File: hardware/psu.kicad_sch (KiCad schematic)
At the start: 35 parts, among them J6 12V Screw Terminal, J7 12V Barrel, Q1 FDS4435BZ, U5 NCP1117-3.3_SOT223, U6 AP64501SP-13

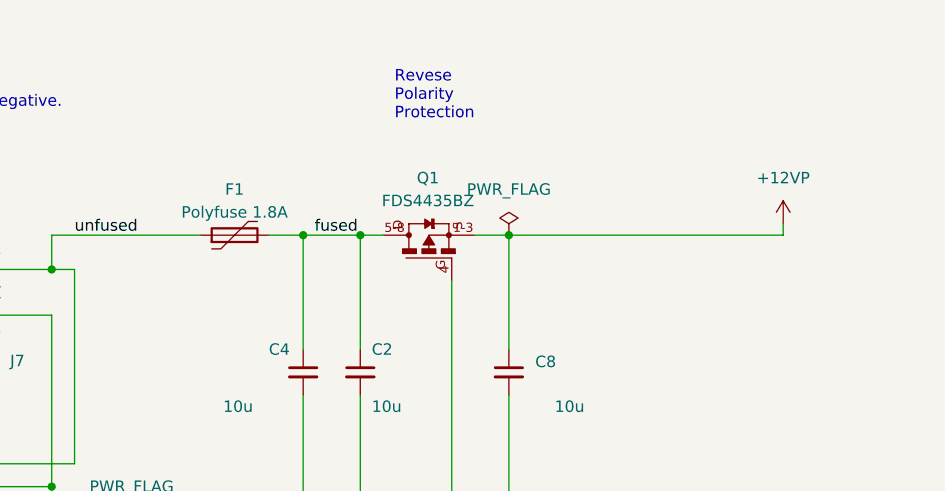
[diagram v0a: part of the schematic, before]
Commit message: PSU: replace polyfuse with SMD fuse (Device:Fuse)
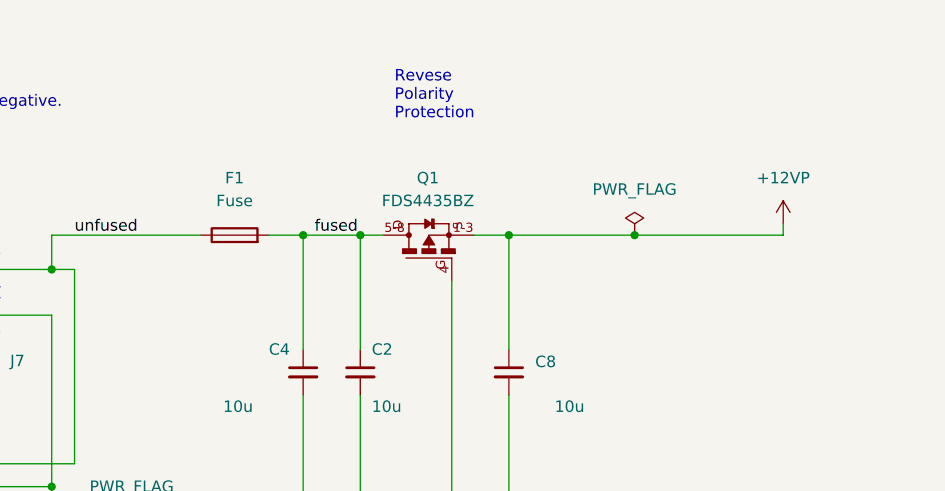
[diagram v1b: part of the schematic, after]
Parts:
- removed F1: Polyfuse 1.8A, Fuse:Fuse_1812_4532Metric, symbol Device:Polyfuse
- added F1: Fuse, symbol Device:Fuse
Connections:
- net fused: now also F1.2
- net unfused: now also F1.1
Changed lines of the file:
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@@
 	)
 	(junction
+		(at 116.84 44.45)
+		(diameter 0)
+		(color 0 0 0 0)
+	)
+	(junction
 		(at 212.09 48.26)
 		(diameter 0)
@@
 	(wire
 		(pts
+			(xy 116.84 44.45) (xy 133.35 44.45)
+		)
+		(stroke
+			(width 0)
+			(type default)
+		)
+	)
+	(wire
+		(pts
 			(xy 179.07 113.03) (xy 179.07 119.38)
 		)
@@
 	(wire
 		(pts
-			(xy 102.87 44.45) (xy 133.35 44.45)
+			(xy 102.87 44.45) (xy 116.84 44.45)
 		)
 		(stroke
@@
 	(symbol
 		(lib_id "power:PWR_FLAG")
-		(at 102.87 44.45 0)
+		(at 116.84 44.45 0)
 		(unit 1)
 		(body_style 1)
@@
 		(fields_autoplaced yes)
 		(property "Reference" "#FLG02"
-			(at 102.87 42.545 0)
+			(at 116.84 42.545 0)
 			(hide yes)
 			(show_name no)
@@
 		)
 		(property "Value" "PWR_FLAG"
-			(at 102.87 39.37 0)
+			(at 116.84 39.37 0)
 			(show_name no)
 			(do_not_autoplace no)
@@
 		)
 		(property "Footprint" ""
-			(at 102.87 44.45 0)
+			(at 116.84 44.45 0)
 			(hide yes)
 			(show_name no)
@@
 		)
 		(property "Datasheet" ""
-			(at 102.87 44.45 0)
+			(at 116.84 44.45 0)
 			(hide yes)
 			(show_name no)
@@
 		)
 		(property "Description" "Special symbol for telling ERC where power comes from"
-			(at 102.87 44.45 0)
+			(at 116.84 44.45 0)
 			(hide yes)
 			(show_name no)
@@
 	)
 	(symbol
-		(lib_id "Device:R_Small")
-		(at 168.91 137.16 0)
+		(lib_id "Device:Fuse")
+		(at 72.39 44.45 90)
 		(unit 1)
 		(body_style 1)
@@
 		(in_pos_files yes)
 		(dnp no)
-		(property "Reference" "R14"
-			(at 170.688 135.9916 0)
+		(fields_autoplaced yes)
+		(property "Reference" "F1"
+			(at 72.39 38.1 90)
 			(show_name no)
 			(do_not_autoplace no)
@@
 					(size 1.27 1.27)
 				)
-				(justify left)
 			)
 		)
-		(property "Value" "20K"
-			(at 170.688 138.303 0)
+		(property "Value" "Fuse"
+			(at 72.39 40.64 90)
 			(show_name no)
 			(do_not_autoplace no)
@@
 					(size 1.27 1.27)
 				)
-				(justify left)
 			)
 		)
-		(property "Footprint" "Resistor_SMD:R_0805_2012Metric"
-			(at 167.132 137.16 90)
+		(property "Footprint" ""
+			(at 72.39 46.228 90)
 			(hide yes)
 			(show_name no)
@@
 		)
 		(property "Datasheet" ""
-			(at 168.91 137.16 0)
-			(hide yes)
-			(show_name no)
-			(do_not_autoplace no)
-			(effects
-				(font
-					(size 1.27 1.27)
-				)
-			)
-		)
-		(property "Description" "Resistor, small symbol"
-			(at 168.91 137.16 0)
-			(hide yes)
-			(show_name no)
-			(do_not_autoplace no)
-			(effects
-				(font
-					(size 1.27 1.27)
-				)
-			)
-		)
-		(property "Notes" "Resistor 20K 1% 63mW"
-			(at 168.91 137.16 0)
+			(at 72.39 44.45 0)
 			(hide yes)
 			(show_name no)
@@
 			)
 		)
-		(property "Supplier" "https://www.digikey.ch/de/products/detail/stackpole-electronics-inc/RMCF0805FT20K0/1760314"
-			(at 168.91 137.16 0)
+		(property "Description" "Fuse"
+			(at 72.39 44.45 0)
 			(hide yes)
 			(show_name no)
@@
 			(project "granit"
 				(path "/d2c135e3-a983-4cd4-8cff-b50ca3c7671a/5c34f141-50d5-4609-a101-f9d94643eff8"
-					(reference "R14")
+					(reference "F1")
 					(unit 1)
 				)
@@
 	)
 	(symbol
-		(lib_id "Device:C_Small")
-		(at 86.36 130.81 0)
+		(lib_id "Device:R_Small")
+		(at 168.91 137.16 0)
 		(unit 1)
 		(body_style 1)
@@
 		(in_pos_files yes)
 		(dnp no)
-		(property "Reference" "C6"
-			(at 89.281 129.6416 0)
+		(property "Reference" "R14"
+			(at 170.688 135.9916 0)
 			(show_name no)
 			(do_not_autoplace no)
@@
 			)
 		)
-		(property "Value" "10u"
-			(at 82.55 136.398 0)
+		(property "Value" "20K"
+			(at 170.688 138.303 0)
 			(show_name no)
 			(do_not_autoplace no)
@@
 			)
 		)
-		(property "Footprint" "Capacitor_SMD:C_0805_2012Metric"
-			(at 87.3252 134.62 0)
+		(property "Footprint" "Resistor_SMD:R_0805_2012Metric"
+			(at 167.132 137.16 90)
 			(hide yes)
 			(show_name no)
@@
 			)
 		)
-		(property "Datasheet" "https://www.samsungsem.com/resources/file/global/support/product_catalog/MLCC.pdf"
-			(at 86.36 130.81 0)
+		(property "Datasheet" ""
+			(at 168.91 137.16 0)
 			(hide yes)
 			(show_name no)
@@
 			)
 		)
-		(property "Description" ""
-			(at 86.36 130.81 0)
+		(property "Description" "Resistor, small symbol"
+			(at 168.91 137.16 0)
 			(hide yes)
 			(show_name no)
@@
 			)
 		)
-		(property "Supplier" "https://www.digikey.ch/de/products/detail/samsung-electro-mechanics/CL21X106KAYNNNE/5961182"
-			(at 86.36 130.81 0)
+		(property "Notes" "Resistor 20K 1% 63mW"
+			(at 168.91 137.16 0)
 			(hide yes)
 			(show_name no)
@@
 			)
 		)
-		(property "Notes" "10% or 20% 35V Ceramic Capacitor X6S 0805 (2012 Metric)"
-			(at 86.36 130.81 0)
+		(property "Supplier" "https://www.digikey.ch/de/products/detail/stackpole-electronics-inc/RMCF0805FT20K0/1760314"
+			(at 168.91 137.16 0)
 			(hide yes)
 			(show_name no)
@@
 			(project "granit"
 				(path "/d2c135e3-a983-4cd4-8cff-b50ca3c7671a/5c34f141-50d5-4609-a101-f9d94643eff8"
-					(reference "C6")
+					(reference "R14")
 					(unit 1)
 				)
@@
 	)
 	(symbol
-		(lib_id "Device:R_Small")
-		(at 135.89 113.03 270)
+		(lib_id "Device:C_Small")
+		(at 86.36 130.81 0)
 		(unit 1)
 		(body_style 1)
@@
 		(in_pos_files yes)
 		(dnp no)
-		(property "Reference" "R13"
-			(at 134.62 109.855 90)
+		(property "Reference" "C6"
+			(at 89.281 129.6416 0)
 			(show_name no)
 			(do_not_autoplace no)
@@
 			)
 		)
-		(property "Value" "10R"
-			(at 134.62 107.95 90)
+		(property "Value" "10u"
+			(at 82.55 136.398 0)
 			(show_name no)
 			(do_not_autoplace no)
@@
 			)
 		)
-		(property "Footprint" "Resistor_SMD:R_0805_2012Metric"
-			(at 135.89 111.252 90)
+		(property "Footprint" "Capacitor_SMD:C_0805_2012Metric"
+			(at 87.3252 134.62 0)
 			(hide yes)
 			(show_name no)
@@
 			)
 		)
-		(property "Datasheet" ""
-			(at 135.89 113.03 0)
+		(property "Datasheet" "https://www.samsungsem.com/resources/file/global/support/product_catalog/MLCC.pdf"
+			(at 86.36 130.81 0)
 			(hide yes)
 			(show_name no)
@@
 			)
 		)
-		(property "Description" "Resistor, small symbol"
-			(at 135.89 113.03 0)
+		(property "Description" ""
+			(at 86.36 130.81 0)
 			(hide yes)
 			(show_name no)
@@
 			)
 		)
-		(property "Notes" "Resistor 10R 1% 63mW"
-			(at 135.89 113.03 0)
+		(property "Supplier" "https://www.digikey.ch/de/products/detail/samsung-electro-mechanics/CL21X106KAYNNNE/5961182"
+			(at 86.36 130.81 0)
 			(hide yes)
 			(show_name no)
@@
 			)
 		)
-		(property "Supplier" "https://www.digikey.ch/de/products/detail/stackpole-electronics-inc/RNCP0805FTD10R0/2240197"
-			(at 135.89 113.03 0)
+		(property "Notes" "10% or 20% 35V Ceramic Capacitor X6S 0805 (2012 Metric)"
+			(at 86.36 130.81 0)
 			(hide yes)
 			(show_name no)
@@
 			(project "granit"
 				(path "/d2c135e3-a983-4cd4-8cff-b50ca3c7671a/5c34f141-50d5-4609-a101-f9d94643eff8"
-					(reference "R13")
+					(reference "C6")
 					(unit 1)
 				)
@@
 	)
 	(symbol
-		(lib_id "Device:Polyfuse")
-		(at 72.39 44.45 90)
+		(lib_id "Device:R_Small")
+		(at 135.89 113.03 270)
 		(unit 1)
 		(body_style 1)
@@
 		(in_pos_files yes)
 		(dnp no)
-		(fields_autoplaced yes)
-		(property "Reference" "F1"
-			(at 72.39 39.37 90)
+		(property "Reference" "R13"
+			(at 134.62 109.855 90)
 			(show_name no)
 			(do_not_autoplace no)
@@
 					(size 1.27 1.27)
 				)
+				(justify left)
 			)
 		)
-		(property "Value" "Polyfuse 1.8A"
-			(at 72.39 41.91 90)
+		(property "Value" "10R"
+			(at 134.62 107.95 90)
 			(show_name no)
 			(do_not_autoplace no)
@@
 					(size 1.27 1.27)
 				)
+				(justify left)
 			)
 		)
-		(property "Footprint" "Fuse:Fuse_1812_4532Metric"
-			(at 77.47 43.18 0)
+		(property "Footprint" "Resistor_SMD:R_0805_2012Metric"
+			(at 135.89 111.252 90)
 			(hide yes)
 			(show_name no)
@@
 					(size 1.27 1.27)
 				)
-				(justify left)
 			)
 		)
-		(property "Datasheet" "https://www.littelfuse.com/~/media/electronics/datasheets/resettable_ptcs/littelfuse_ptc_1812l_datasheet.pdf.pdf"
-			(at 72.39 44.45 0)
+		(property "Datasheet" ""
+			(at 135.89 113.03 0)
 			(hide yes)
 			(show_name no)
@@
 			)
 		)
-		(property "Description" ""
-			(at 72.39 44.45 0)
+		(property "Description" "Resistor, small symbol"
+			(at 135.89 113.03 0)
 			(hide yes)
 			(show_name no)
@@
 			)
 		)
-		(property "Supplier" "https://www.digikey.ch/de/products/detail/littelfuse-inc/1812L150-24MR/2023969"
-			(at 72.39 44.45 90)
+		(property "Notes" "Resistor 10R 1% 63mW"
+			(at 135.89 113.03 0)
+			(hide yes)
+			(show_name no)
+			(do_not_autoplace no)
+			(effects
+				(font
+					(size 1.27 1.27)
+				)
+			)
+		)
+		(property "Supplier" "https://www.digikey.ch/de/products/detail/stackpole-electronics-inc/RNCP0805FTD10R0/2240197"
+			(at 135.89 113.03 0)
 			(hide yes)
 			(show_name no)
@@
 			(project "granit"
 				(path "/d2c135e3-a983-4cd4-8cff-b50ca3c7671a/5c34f141-50d5-4609-a101-f9d94643eff8"
-					(reference "F1")
+					(reference "R13")
 					(unit 1)
 				)

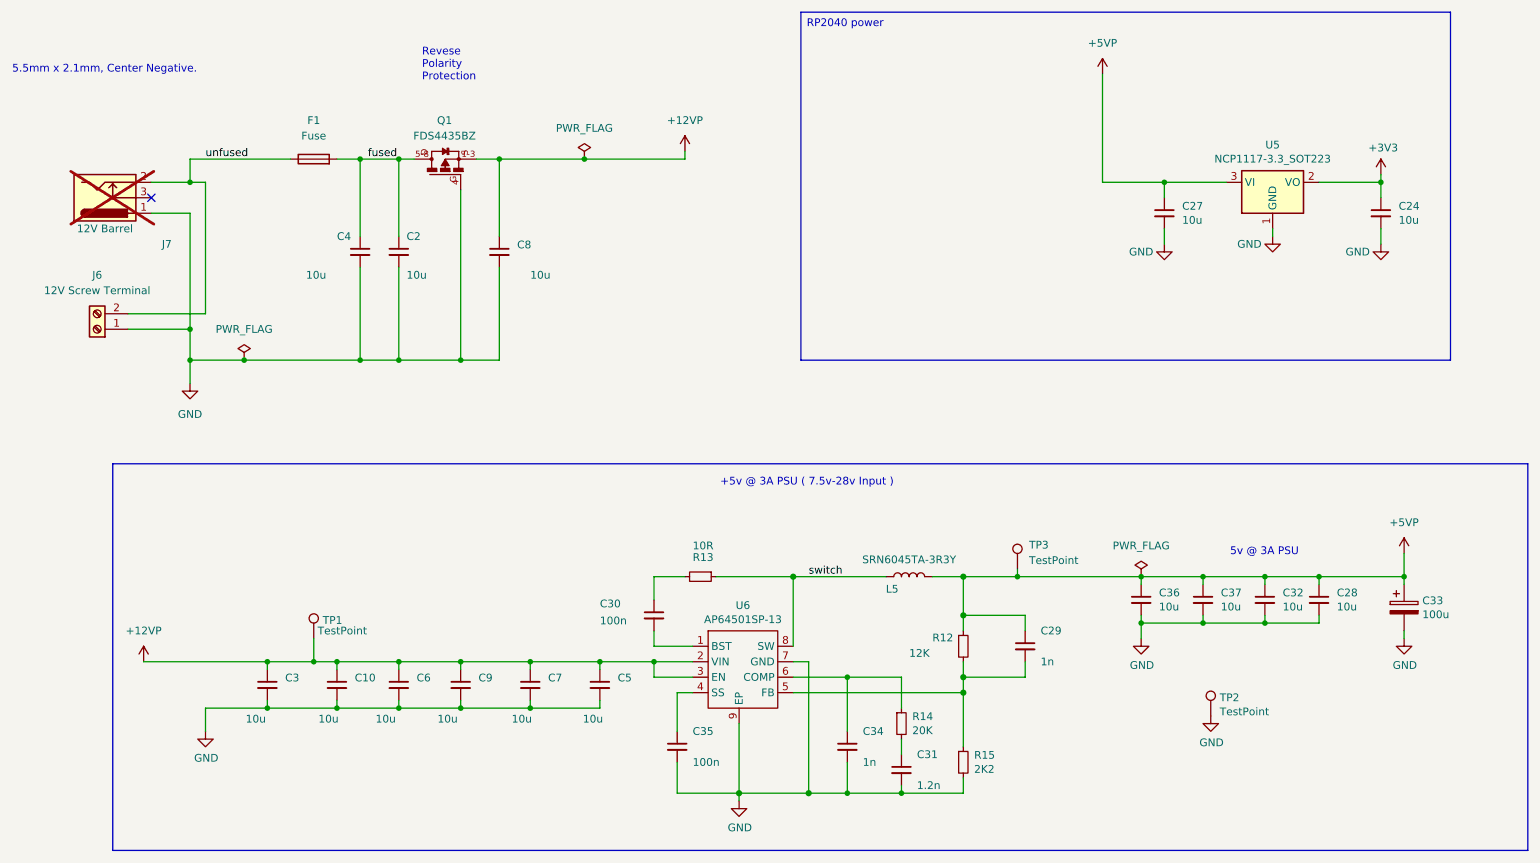
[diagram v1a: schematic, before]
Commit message: Reannotate all components sequentially
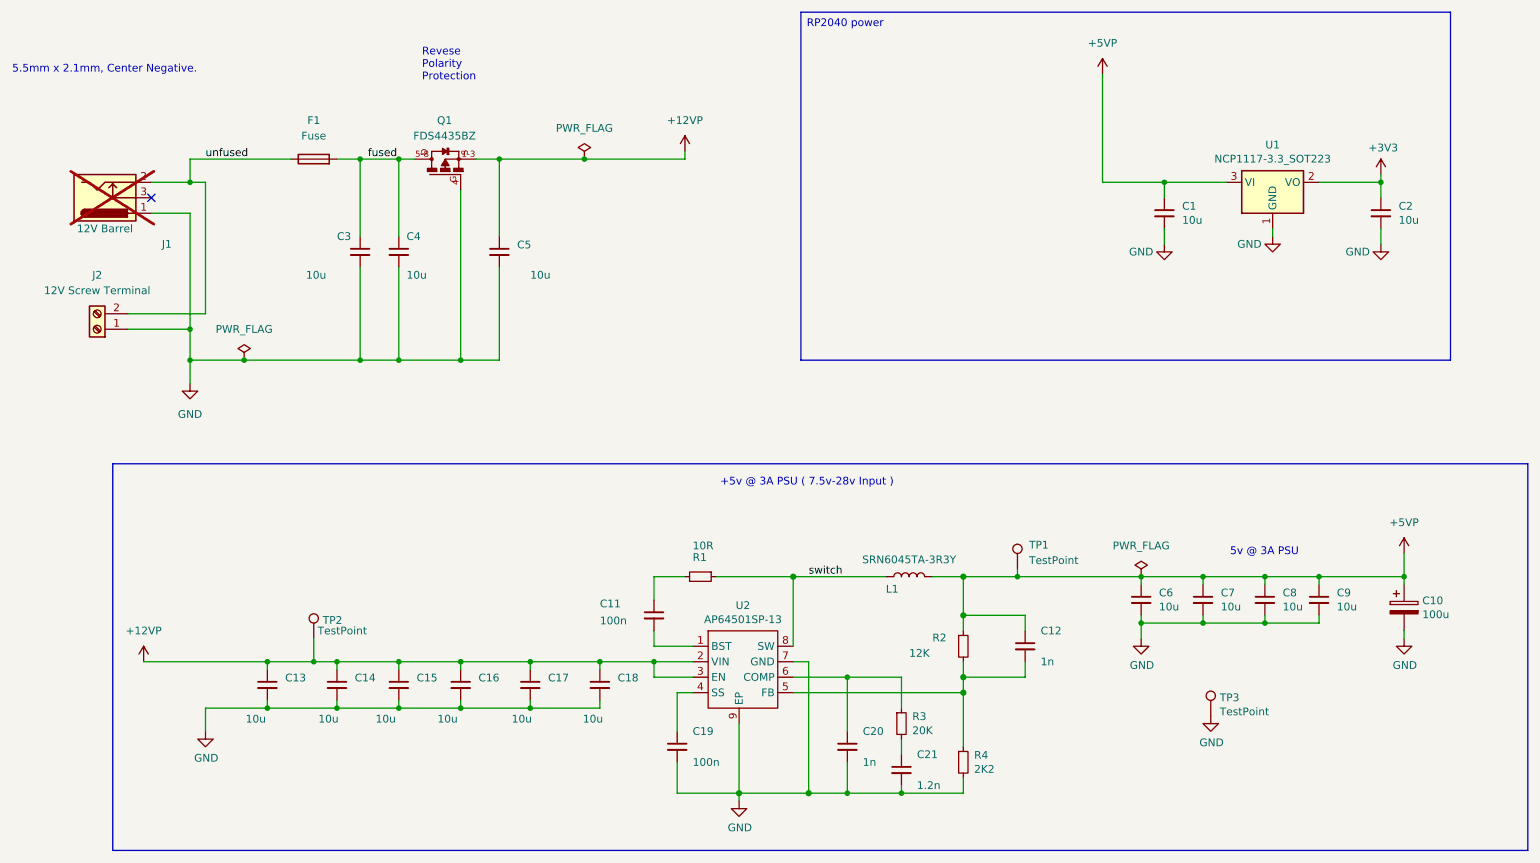
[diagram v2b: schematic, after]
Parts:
- renumbered C27 to C1, C33 to C10, C30 to C11, C29 to C12, C3 to C13, C10 to C14, C6 to C15, C9 to C16, C7 to C17, C5 to C18, C35 to C19, C24 to C2, C34 to C20, C31 to C21, C4 to C3, C2 to C4, C8 to C5, C36 to C6, C37 to C7, C32 to C8, C28 to C9, J7 to J1, J6 to J2, L5 to L1, R13 to R1, R12 to R2, R14 to R3, R15 to R4, TP3 to TP1, TP1 to TP2, TP2 to TP3, U5 to U1, U6 to U2

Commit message: Assign footprints to all components
All components now have valid footprints:
- 0805 for all resistors, caps, LEDs
- SOT-23-5/6 for ICs
- 2512 SMD fuse, 3215 crystal
- Pin headers, USB-C, solder jumper, battery holder
- ERC: 0 errors, 0 warnings
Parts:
- F1: footprint (none) -> Fuse:Fuse_2512_6332Metric
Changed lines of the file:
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@@
 			)
 		)
-		(property "Footprint" ""
+		(property "Footprint" "Resistor_SMD:R_0805_2012Metric"
 			(at 52.07 81.28 0)
 			(hide yes)
@@
 			)
 		)
-		(property "Footprint" ""
+		(property "Footprint" "Fuse:Fuse_2512_6332Metric"
 			(at 72.39 46.228 90)
 			(hide yes)
@@
 			)
 		)
-		(property "Footprint" ""
+		(property "Footprint" "Resistor_SMD:R_0805_2012Metric"
 			(at 54.61 138.43 0)
 			(hide yes)
@@
 			)
 		)
-		(property "Footprint" ""
+		(property "Footprint" "Resistor_SMD:R_0805_2012Metric"
 			(at 247.65 46.99 0)
 			(hide yes)
